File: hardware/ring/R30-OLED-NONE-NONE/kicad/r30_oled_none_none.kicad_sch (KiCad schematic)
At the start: 0 parts

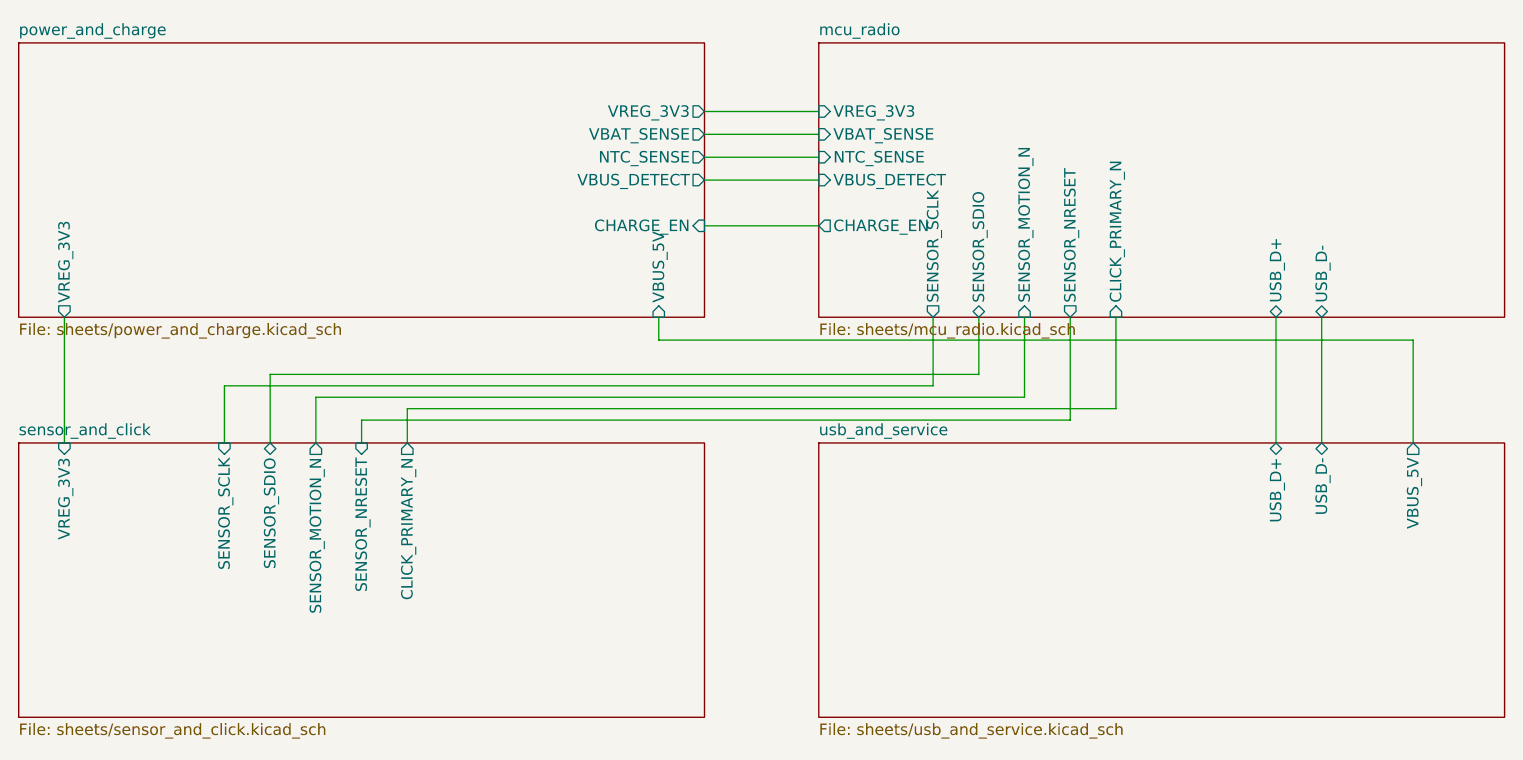
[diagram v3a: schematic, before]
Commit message: fix(r30): clean schematic erc library baseline
Design disclosure: sensing mechanism PAW3204-class optical tracking; form factor R30-OLED-NONE-NONE fingertip ring, active 30-degree ring packet; intended use BLE HID pointing for accessibility; BOM estimate ~$5.30-9.45.

Materialize the project-local PowerFinger symbol and PowerFinger_Ring footprint libraries, wire sheet-interface labels, keep PAW3204 reset/motion local to sensor test pads, and update the verified KiCad snapshot to ERC=0, DRC=349, unconnected=41, parity=118.
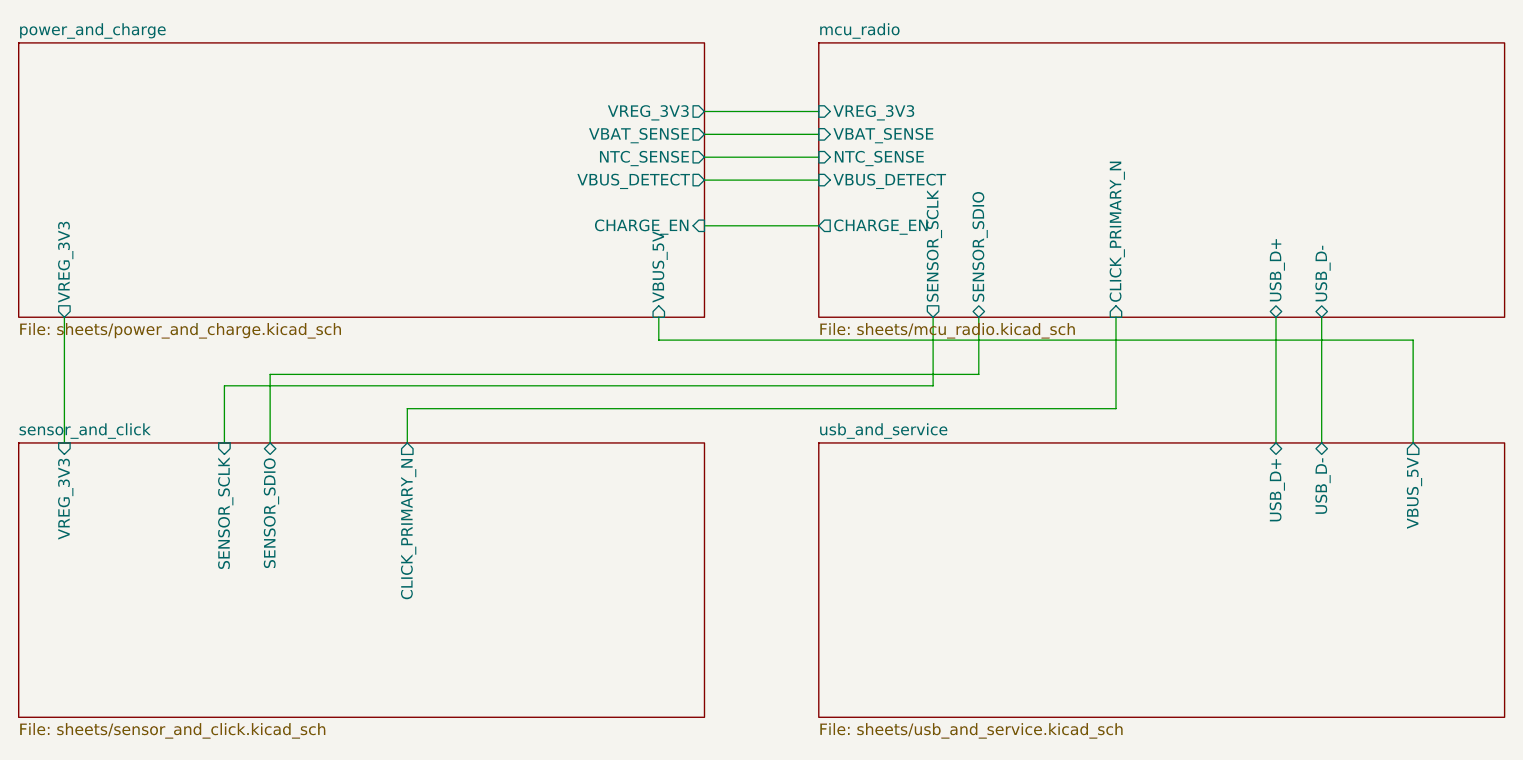
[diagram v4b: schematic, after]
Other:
- sheet mcu_radio ports: added none; removed SENSOR_MOTION_N, SENSOR_NRESET
- sheet sensor_and_click ports: added none; removed SENSOR_MOTION_N, SENSOR_NRESET
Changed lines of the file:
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@@
       (effects (font (size 1.27 1.27)) (justify left))
     )
-    (pin "SENSOR_MOTION_N" input (at 137.16 55.88 270)
-      (effects (font (size 1.27 1.27)) (justify left))
-    )
-    (pin "SENSOR_NRESET" output (at 142.24 55.88 270)
-      (effects (font (size 1.27 1.27)) (justify left))
-    )
-    (pin "CLICK_PRIMARY_N" input (at 147.32 55.88 270)
+            (pin "CLICK_PRIMARY_N" input (at 147.32 55.88 270)
       (effects (font (size 1.27 1.27)) (justify left))
     )
@@
       (effects (font (size 1.27 1.27)) (justify right))
     )
-    (pin "SENSOR_MOTION_N" output (at 58.42 69.85 90)
-      (effects (font (size 1.27 1.27)) (justify right))
-    )
-    (pin "SENSOR_NRESET" input (at 63.5 69.85 90)
-      (effects (font (size 1.27 1.27)) (justify right))
-    )
-    (pin "CLICK_PRIMARY_N" output (at 68.58 69.85 90)
+            (pin "CLICK_PRIMARY_N" output (at 68.58 69.85 90)
       (effects (font (size 1.27 1.27)) (justify right))
     )
@@
     (stroke (width 0) (type default) (color 0 0 0 0))
   )
-  (wire
-    (pts
-      (xy 58.42 69.85)
-      (xy 58.42 64.77)
-    )
-    (stroke (width 0) (type default) (color 0 0 0 0))
-  )
-  (wire
-    (pts
-      (xy 58.42 64.77)
-      (xy 137.16 64.77)
-    )
-    (stroke (width 0) (type default) (color 0 0 0 0))
-  )
-  (wire
-    (pts
-      (xy 137.16 64.77)
-      (xy 137.16 55.88)
-    )
-    (stroke (width 0) (type default) (color 0 0 0 0))
-  )
-  (wire
-    (pts
-      (xy 63.5 69.85)
-      (xy 63.5 67.31)
-    )
-    (stroke (width 0) (type default) (color 0 0 0 0))
-  )
-  (wire
-    (pts
-      (xy 63.5 67.31)
-      (xy 142.24 67.31)
-    )
-    (stroke (width 0) (type default) (color 0 0 0 0))
-  )
-  (wire
-    (pts
-      (xy 142.24 67.31)
-      (xy 142.24 55.88)
-    )
-    (stroke (width 0) (type default) (color 0 0 0 0))
-  )
-  (wire
+              (wire
     (pts
       (xy 68.58 69.85)

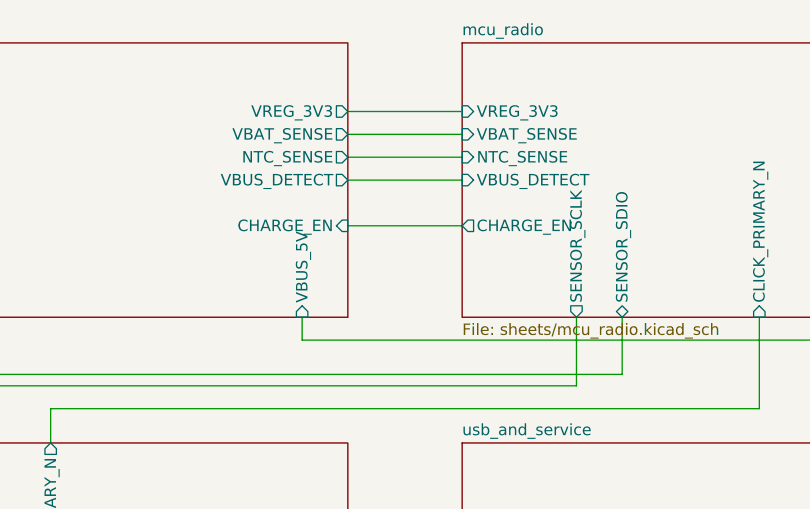
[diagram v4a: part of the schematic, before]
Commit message: feat(r30): cut service hardware blockers
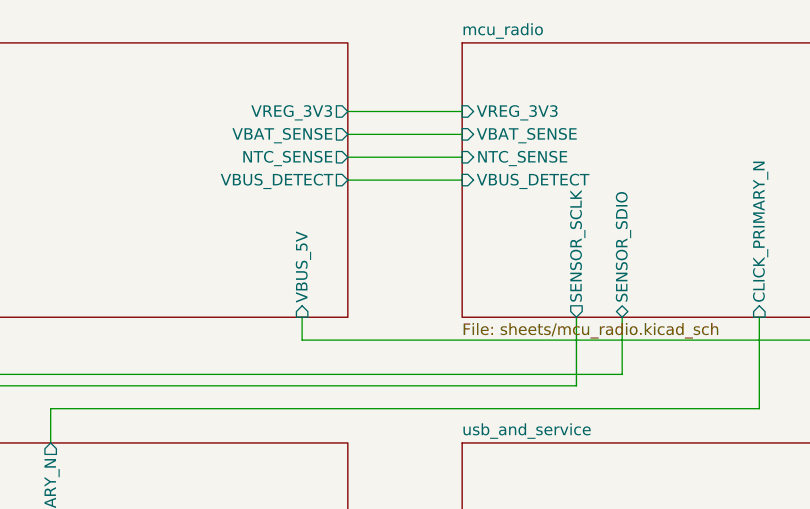
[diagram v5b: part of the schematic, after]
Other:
- sheet mcu_radio ports: added none; removed CHARGE_EN
- sheet power_and_charge ports: added none; removed CHARGE_EN
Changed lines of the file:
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@@
-      (effects (font (size 1.27 1.27)) (justify right))
-    )
-    (pin "CHARGE_EN" input (at 101.6 45.72 0)
       (effects (font (size 1.27 1.27)) (justify right))
     )
@@
     )
     (pin "VBUS_DETECT" input (at 114.3 40.64 180)
-      (effects (font (size 1.27 1.27)) (justify left))
-    )
-    (pin "CHARGE_EN" output (at 114.3 45.72 180)
       (effects (font (size 1.27 1.27)) (justify left))
     )
@@
     )
     (stroke (width 0) (type default) (color 0 0 0 0))
-  )
-  (wire
-    (pts
-      (xy 101.6 45.72)
-      (xy 114.3 45.72)
-    )
-    (stroke (width 0) (type default) (color 0 0 0 0))
